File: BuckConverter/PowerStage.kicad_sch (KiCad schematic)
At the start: 11 parts, among them J1 Conn_01x01_Pin, J2 Conn_01x01_Pin, J3 Conn_01x01_Pin, J4 Conn_01x01_Pin, J5 Conn_01x01_Pin, Q1 IRF540N

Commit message: PCB Completed
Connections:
- net Vout is gone; now on net VOUT: J3.1 (Pin_1)
- net GND: now also C3.2, C4.2, C5.2, D1.2 (A)
- net VIN: now also C3.1, C4.1, Q1.2 (D)
- net VOUT: now also C5.1, L1.2
- net VSW: now also D1.1 (K), L1.1, Q1.3 (S)
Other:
- moved on the sheet: L1
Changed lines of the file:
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@@
-	)
-	(junction
-		(at 130.81 33.02)
-		(diameter 0)
-		(color 0 0 0 0)
 	)
 	(junction
@@
 	(wire
 		(pts
-			(xy 130.81 33.02) (xy 130.81 25.4)
-		)
-		(stroke
-			(width 0)
-			(type default)
-		)
-	)
-	(wire
-		(pts
 			(xy 116.84 25.4) (xy 116.84 44.45)
 		)
@@
 	(wire
 		(pts
-			(xy 130.81 48.26) (xy 149.86 48.26)
-		)
-		(stroke
-			(width 0)
-			(type default)
-		)
-	)
-	(wire
-		(pts
-			(xy 130.81 34.29) (xy 130.81 33.02)
+			(xy 149.86 48.26) (xy 157.48 48.26)
+		)
+		(stroke
+			(width 0)
+			(type default)
+		)
+	)
+	(wire
+		(pts
+			(xy 130.81 48.26) (xy 142.24 48.26)
+		)
+		(stroke
+			(width 0)
+			(type default)
+		)
+	)
+	(wire
+		(pts
+			(xy 130.81 25.4) (xy 130.81 33.02)
 		)
 		(stroke
@@
 	(wire
 		(pts
+			(xy 157.48 48.26) (xy 157.48 53.34)
+		)
+		(stroke
+			(width 0)
+			(type default)
+		)
+	)
+	(wire
+		(pts
 			(xy 102.87 60.96) (xy 116.84 60.96)
 		)
@@
 		(pts
 			(xy 102.87 25.4) (xy 102.87 44.45)
-		)
-		(stroke
-			(width 0)
-			(type default)
-		)
-	)
-	(wire
-		(pts
-			(xy 157.48 48.26) (xy 157.48 53.34)
 		)
 		(stroke
@@
 	(rectangle
 		(start 96.52 16.51)
-		(end 163.83 63.5)
+		(end 165.1 71.12)
 		(stroke
 			(width 0)
@@
 		)
 	)
+	(label "VIN"
+		(at 130.81 25.4 0)
+		(effects
+			(font
+				(size 1.27 1.27)
+			)
+			(justify left bottom)
+		)
+	)
 	(label "VG"
 		(at 24.13 22.86 0)
@@
 		)
 	)
-	(label "Vout"
+	(label "VOUT"
 		(at 72.39 62.23 0)
 		(effects
@@
 		)
 	)
+	(label "VSW"
+		(at 130.81 48.26 180)
+		(effects
+			(font
+				(size 1.27 1.27)
+			)
+			(justify right bottom)
+		)
+	)
 	(label "VG"
 		(at 123.19 38.1 180)
@@
 	(label "VIN"
 		(at 36.83 60.96 0)
+		(effects
+			(font
+				(size 1.27 1.27)
+			)
+			(justify left bottom)
+		)
+	)
+	(label "VOUT"
+		(at 157.48 48.26 0)
 		(effects
 			(font
@@
 	(symbol
 		(lib_id "Device:L")
-		(at 153.67 48.26 90)
+		(at 146.05 48.26 90)
 		(unit 1)
 		(exclude_from_sim no)
@@
 		(fields_autoplaced yes)
 		(property "Reference" "L1"
-			(at 153.67 43.18 90)
+			(at 146.05 43.18 90)
 			(effects
 				(font
@@
 		)
 		(property "Value" "?"
-			(at 153.67 45.72 90)
+			(at 146.05 45.72 90)
 			(effects
 				(font
@@
 		)
 		(property "Footprint" "Inductor_THT:L_Radial_D50.8mm_P38.86mm_Vishay_IHB-6"
-			(at 153.67 48.26 0)
+			(at 146.05 48.26 0)
 			(effects
 				(font
@@
 		)
 		(property "Datasheet" "~"
-			(at 153.67 48.26 0)
+			(at 146.05 48.26 0)
 			(effects
 				(font
@@
 		)
 		(property "Description" "Inductor"
-			(at 153.67 48.26 0)
+			(at 146.05 48.26 0)
 			(effects
 				(font
@@
 		)
 		(property "Part Number" "?"
-			(at 153.67 48.26 0)
+			(at 146.05 48.26 0)
 			(effects
 				(font
@@
 					(unit 1)
 				)
+			)
+		)
+	)
+	(symbol
+		(lib_id "power:GND")
+		(at 116.84 60.96 0)
+		(unit 1)
+		(exclude_from_sim no)
+		(in_bom yes)
+		(on_board yes)
+		(dnp no)
+		(fields_autoplaced yes)
+		(property "Reference" "#PWR055"
+			(at 116.84 67.31 0)
+			(effects
+				(font
+					(size 1.27 1.27)
+				)
+				(hide yes)
+			)
+		)
+		(property "Value" "GND"
+			(at 116.84 66.04 0)
+			(effects
+				(font
+					(size 1.27 1.27)
+				)
+			)
+		)
+		(property "Footprint" ""
+			(at 116.84 60.96 0)
+			(effects
+				(font
+					(size 1.27 1.27)
+				)
+				(hide yes)
+			)
+		)
+		(property "Datasheet" ""
+			(at 116.84 60.96 0)
+			(effects
+				(font
+					(size 1.27 1.27)
+				)
+				(hide yes)
+			)
+		)
+		(property "Description" "Power symbol creates a global label with name \"GND\" , ground"
+			(at 116.84 60.96 0)
+			(effects
+				(font
+					(size 1.27 1.27)
+				)
+				(hide yes)
+			)
+		)
+		(pin "1"
+		)
+		(instances
+			(project "BuckConverter"
+				(path "/fd6bac42-b74a-4329-b064-b676c79abc2c/e19e5572-51cf-4547-aaae-cb2f4f587423"
+					(reference "#PWR055")
+					(unit 1)
+				)

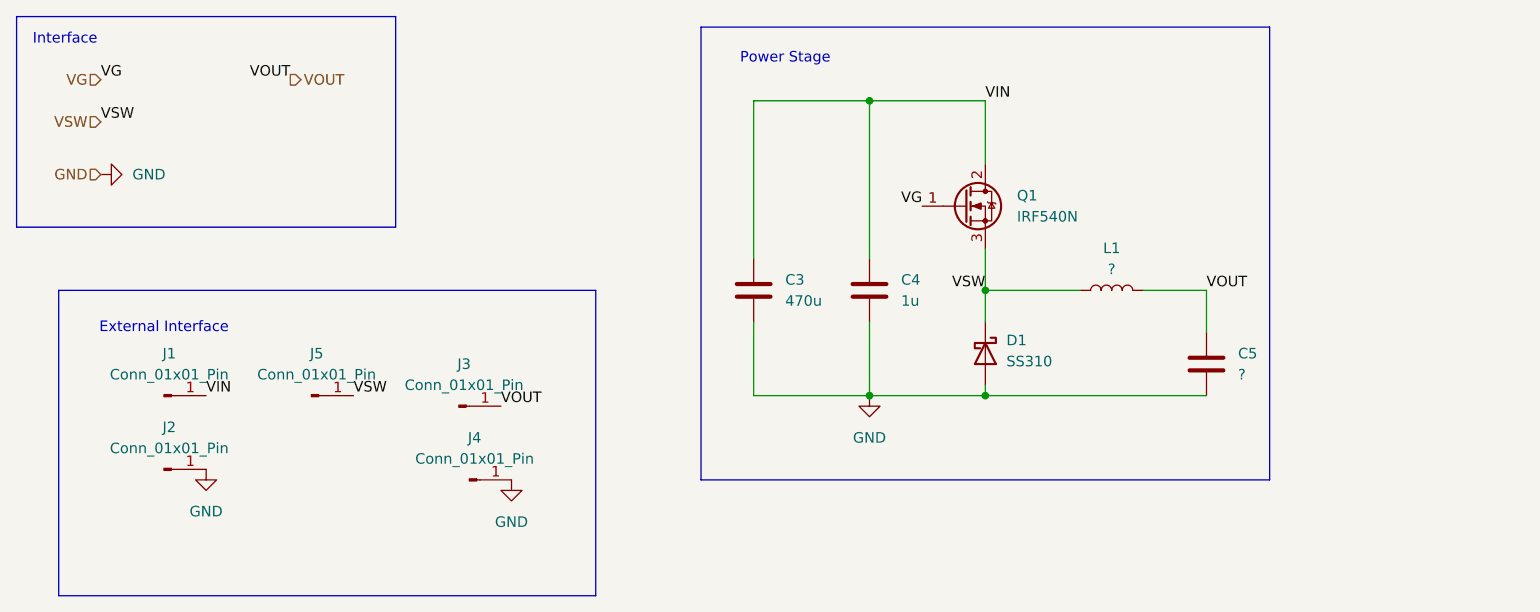
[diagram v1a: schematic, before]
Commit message: PCB updated LC footprints
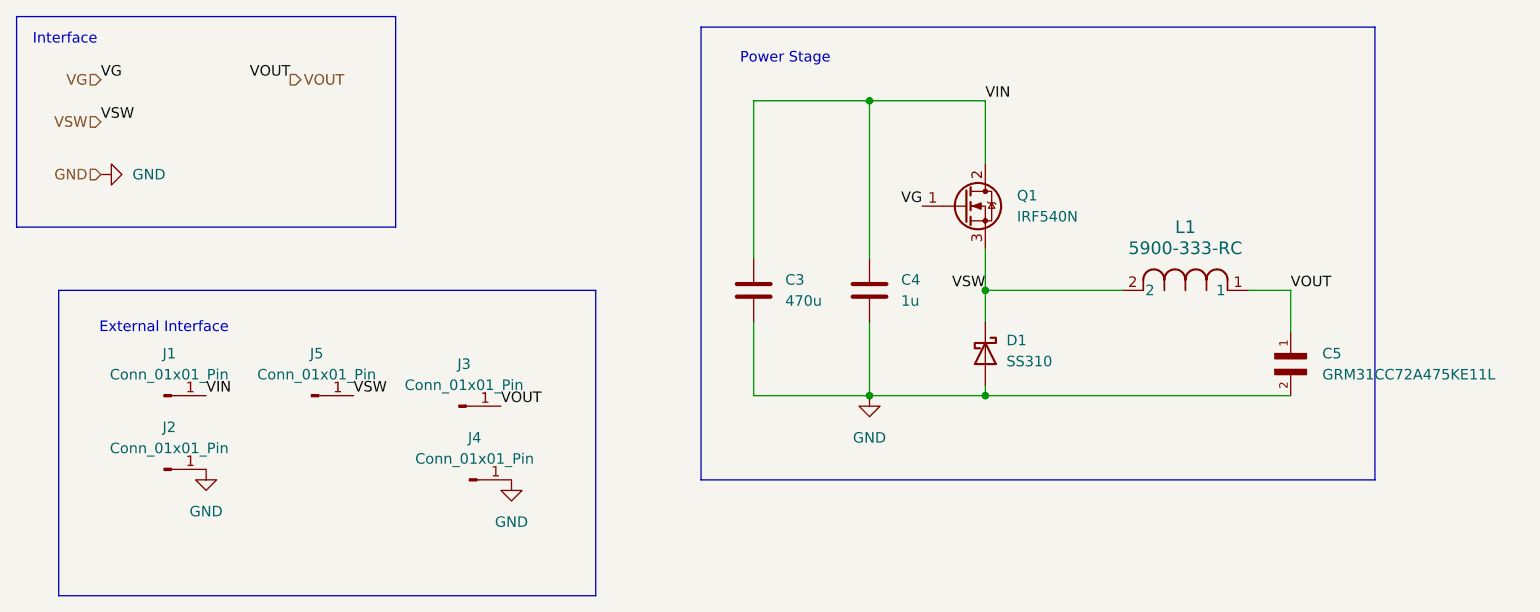
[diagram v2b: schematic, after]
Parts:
- removed C5: ?, Capacitor_THT:CP_Radial_D18.0mm_P7.50mm, symbol Device:C
- removed L1: ?, Inductor_THT:L_Radial_D50.8mm_P38.86mm_Vishay_IHB-6, symbol Device:L
- added C5: GRM31CC72A475KE11L, GRM31CC72A475KE11L:CAPC3216X190N, symbol GRM31CC72A475KE11L:GRM31CC72A475KE11L
- added L1: 5900-333-RC, IND_BOURNS_5900, symbol 5900-333-RC:5900-333-RC
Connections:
- net GND: now also C5.2
- net VOUT: now also C5.1, L1.1
- net VSW: now also L1.2
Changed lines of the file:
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@@
 	(wire
 		(pts
-			(xy 130.81 60.96) (xy 157.48 60.96)
+			(xy 130.81 60.96) (xy 167.64 60.96)
 		)
 		(stroke
@@
 	(wire
 		(pts
-			(xy 149.86 48.26) (xy 157.48 48.26)
-		)
-		(stroke
-			(width 0)
-			(type default)
-		)
-	)
-	(wire
-		(pts
-			(xy 130.81 48.26) (xy 142.24 48.26)
+			(xy 162.56 48.26) (xy 167.64 48.26)
+		)
+		(stroke
+			(width 0)
+			(type default)
+		)
+	)
+	(wire
+		(pts
+			(xy 130.81 48.26) (xy 147.32 48.26)
 		)
 		(stroke
@@
 	(wire
 		(pts
-			(xy 157.48 48.26) (xy 157.48 53.34)
+			(xy 167.64 48.26) (xy 167.64 53.34)
 		)
 		(stroke
@@
 	(rectangle
 		(start 96.52 16.51)
-		(end 165.1 71.12)
+		(end 177.8 71.12)
 		(stroke
 			(width 0)
@@
 	)
 	(label "VOUT"
-		(at 157.48 48.26 0)
+		(at 167.64 48.26 0)
 		(effects
 			(font
@@
 	)
 	(symbol
-		(lib_id "Device:C")
-		(at 157.48 57.15 0)
-		(unit 1)
-		(exclude_from_sim no)
-		(in_bom yes)
-		(on_board yes)
-		(dnp no)
-		(fields_autoplaced yes)
-		(property "Reference" "C5"
-			(at 161.29 55.8799 0)
-			(effects
-				(font
-					(size 1.27 1.27)
-				)
-				(justify left)
-			)
-		)
-		(property "Value" "?"
-			(at 161.29 58.4199 0)
-			(effects
-				(font
-					(size 1.27 1.27)
-				)
-				(justify left)
-			)
-		)
-		(property "Footprint" "Capacitor_THT:CP_Radial_D18.0mm_P7.50mm"
-			(at 158.4452 60.96 0)
-			(effects
-				(font
-					(size 1.27 1.27)
-				)
-				(hide yes)
-			)
-		)
-		(property "Datasheet" "~"
-			(at 157.48 57.15 0)
-			(effects
-				(font
-					(size 1.27 1.27)
-				)
-				(hide yes)
-			)
-		)
-		(property "Description" "Electrolythic Capacitor"
-			(at 157.48 57.15 0)
-			(effects
-				(font
-					(size 1.27 1.27)
-				)
-				(hide yes)
-			)
-		)
-		(property "Part Number" "?"
-			(at 157.48 57.15 0)
-			(effects
-				(font
-					(size 1.27 1.27)
-				)
-				(hide yes)
-			)
-		)
-		(pin "1"
-		)
-		(pin "2"
-		)
-		(instances
-			(project "BuckConverter"
-				(path "/fd6bac42-b74a-4329-b064-b676c79abc2c/e19e5572-51cf-4547-aaae-cb2f4f587423"
-					(reference "C5")
-					(unit 1)
-				)
-			)
-		)
-	)
-	(symbol
 		(lib_id "Transistor_FET:IRF540N")
 		(at 128.27 38.1 0)
@@
 	)
 	(symbol
+		(lib_id "GRM31CC72A475KE11L:GRM31CC72A475KE11L")
+		(at 167.64 55.88 270)
+		(unit 1)
+		(exclude_from_sim no)
+		(in_bom yes)
+		(on_board yes)
+		(dnp no)
+		(fields_autoplaced yes)
+		(property "Reference" "C5"
+			(at 171.45 55.8799 90)
+			(effects
+				(font
+					(size 1.27 1.27)
+				)
+				(justify left)
+			)
+		)
+		(property "Value" "GRM31CC72A475KE11L"
+			(at 171.45 58.4199 90)
+			(effects
+				(font
+					(size 1.27 1.27)
+				)
+				(justify left)
+			)
+		)
+		(property "Footprint" "GRM31CC72A475KE11L:CAPC3216X190N"
+			(at 167.64 55.88 0)
+			(effects
+				(font
+					(size 1.27 1.27)
+				)
+				(justify bottom)
+				(hide yes)
+			)
+		)
+		(property "Datasheet" ""
+			(at 167.64 55.88 0)
+			(effects
+				(font
+					(size 1.27 1.27)
+				)
+				(hide yes)
+			)
+		)
+		(property "Description" ""
+			(at 167.64 55.88 0)
+			(effects
+				(font
+					(size 1.27 1.27)
+				)
+				(hide yes)
+			)
+		)
+		(pin "1"
+		)
+		(pin "2"
+		)
+		(instances
+			(project ""
+				(path "/fd6bac42-b74a-4329-b064-b676c79abc2c/e19e5572-51cf-4547-aaae-cb2f4f587423"
+					(reference "C5")
+					(unit 1)
+				)
+			)
+		)
+	)
+	(symbol
 		(lib_id "Connector:Conn_01x01_Pin")
 		(at 31.75 69.85 0)
@@
 	)
 	(symbol
-		(lib_id "Device:L")
-		(at 146.05 48.26 90)
-		(unit 1)
-		(exclude_from_sim no)
-		(in_bom yes)
-		(on_board yes)
-		(dnp no)
-		(fields_autoplaced yes)
-		(property "Reference" "L1"
-			(at 146.05 43.18 90)
-			(effects
-				(font
-					(size 1.27 1.27)
-				)
-			)
-		)
-		(property "Value" "?"
-			(at 146.05 45.72 90)
-			(effects
-				(font
-					(size 1.27 1.27)
-				)
-			)
-		)
-		(property "Footprint" "Inductor_THT:L_Radial_D50.8mm_P38.86mm_Vishay_IHB-6"
-			(at 146.05 48.26 0)
-			(effects
-				(font
-					(size 1.27 1.27)
-				)
-				(hide yes)
-			)
-		)
-		(property "Datasheet" "~"
-			(at 146.05 48.26 0)
-			(effects
-				(font
-					(size 1.27 1.27)
-				)
-				(hide yes)
-			)
-		)
-		(property "Description" "Inductor"
-			(at 146.05 48.26 0)
-			(effects
-				(font
-					(size 1.27 1.27)
-				)
-				(hide yes)
-			)
-		)
-		(property "Part Number" "?"
-			(at 146.05 48.26 0)
-			(effects
-				(font
-					(size 1.27 1.27)
-				)
-				(hide yes)
-			)
-		)
-		(pin "2"
-		)
-		(pin "1"
-		)
-		(instances
-			(project ""
-				(path "/fd6bac42-b74a-4329-b064-b676c79abc2c/e19e5572-51cf-4547-aaae-cb2f4f587423"
-					(reference "L1")
-					(unit 1)
-				)
-			)
-		)
-	)
-	(symbol
 		(lib_id "Connector:Conn_01x01_Pin")
 		(at 68.58 71.12 0)
@@
 					(unit 1)
 				)
+			)
+		)
+	)
+	(symbol
+		(lib_id "5900-333-RC:5900-333-RC")
+		(at 147.32 48.26 0)
+		(unit 1)
+		(exclude_from_sim no)
+		(in_bom yes)
+		(on_board yes)
+		(dnp no)
+		(fields_autoplaced yes)
+		(property "Reference" "L1"
+			(at 154.94 40.64 0)
+			(effects
+				(font
+					(size 1.524 1.524)
+				)
+			)
+		)
+		(property "Value" "5900-333-RC"
+			(at 154.94 43.18 0)
+			(effects
+				(font
+					(size 1.524 1.524)
+				)
+			)
+		)
+		(property "Footprint" "IND_BOURNS_5900"
+			(at 147.32 48.26 0)
+			(effects
+				(font
+					(size 1.27 1.27)
+					(italic yes)
+				)
+				(hide yes)
+			)
+		)
+		(property "Datasheet" "5900-333-RC"
+			(at 147.32 48.26 0)
+			(effects
+				(font
+					(size 1.27 1.27)
+					(italic yes)
+				)
+				(hide yes)
+			)
+		)
+		(property "Description" ""
+			(at 147.32 48.26 0)
+			(effects
+				(font
+					(size 1.27 1.27)
+				)
+				(hide yes)
+			)
+		)
+		(pin "2"
+		)
+		(pin "1"
+		)
+		(instances
+			(project ""
+				(path "/fd6bac42-b74a-4329-b064-b676c79abc2c/e19e5572-51cf-4547-aaae-cb2f4f587423"
+					(reference "L1")
+					(unit 1)
+				)

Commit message: updated BOM
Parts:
- C5: value GRM31CC72A475KE11L -> 4.7 µF; Part Number (none) -> GRM31CC72A475KE11L
- L1: value 5900-333-RC -> 33mH; Part Number (none) -> 5900-333-RC
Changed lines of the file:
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@@
 			)
 		)
-		(property "Value" "GRM31CC72A475KE11L"
+		(property "Value" "4.7 µF"
 			(at 171.45 58.4199 90)
 			(effects
@@
 			)
 		)
+		(property "Part Number" "GRM31CC72A475KE11L"
+			(at 167.64 55.88 90)
+			(effects
+				(font
+					(size 1.27 1.27)
+				)
+				(hide yes)
+			)
+		)
 		(pin "1"
 		)
@@
 			)
 		)
-		(property "Value" "5900-333-RC"
+		(property "Value" "33mH"
 			(at 154.94 43.18 0)
 			(effects
@@
 			(at 147.32 48.26 0)
 			(effects
+				(font
+					(size 1.27 1.27)
+				)
+				(hide yes)
+			)
+		)
+		(property "Part Number" "5900-333-RC"
+			(at 147.32 48.26 0)
+			(effects
